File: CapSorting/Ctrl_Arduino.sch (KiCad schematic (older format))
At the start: 18 parts, among them U12 TLP785, U13 TLP785

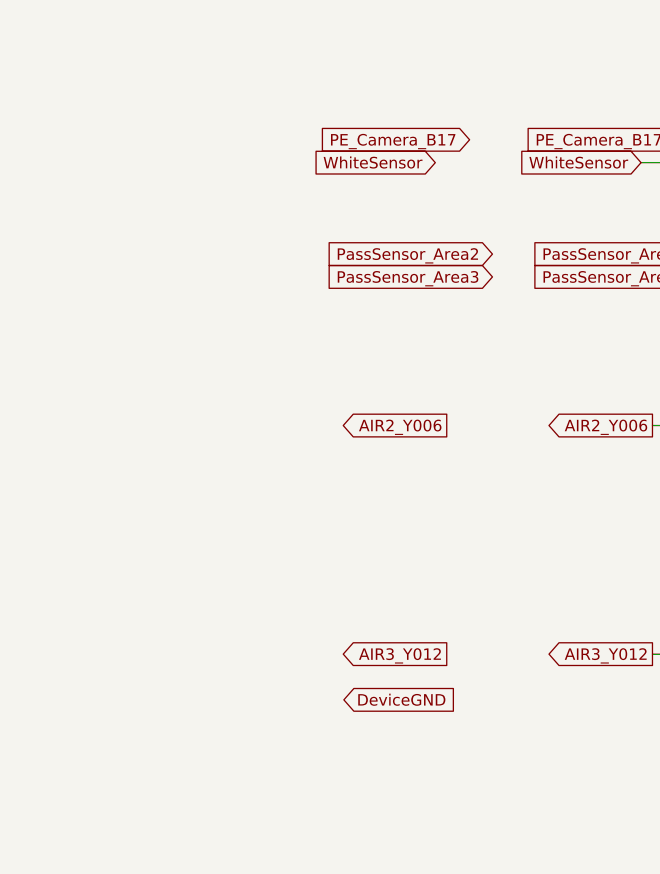
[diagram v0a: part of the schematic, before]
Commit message: Arduino回路図　コネクタ追加
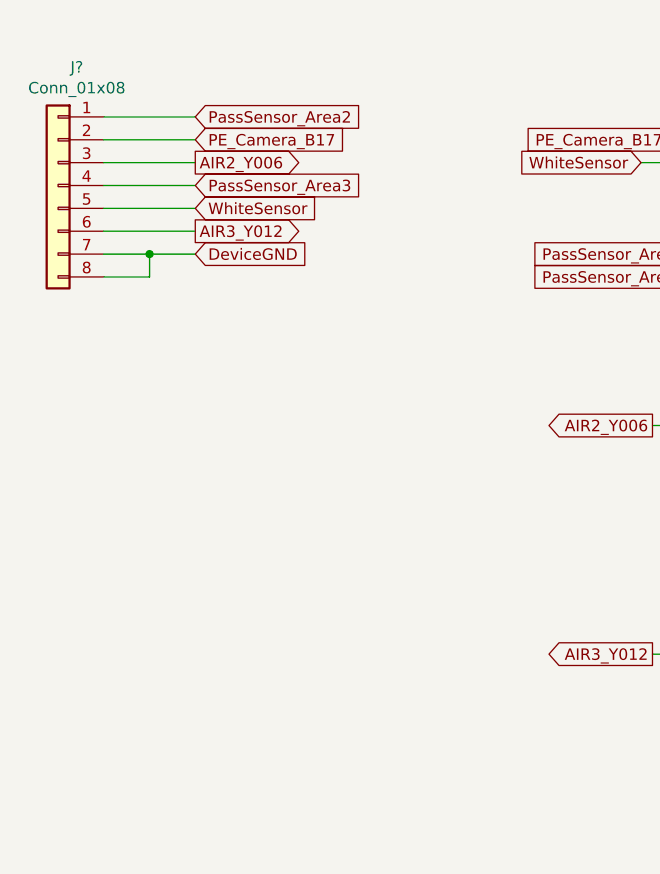
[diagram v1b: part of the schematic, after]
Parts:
- added J?: Conn_01x08, symbol Connector_Generic:Conn_01x08
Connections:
- net AIR2_Y006: now also J?.3 (Pin_3)
- net AIR3_Y012: now also J?.6 (Pin_6)
- net DeviceGND: now also J?.7 (Pin_7), J?.8 (Pin_8)
- net PE_Camera_B17: now also J?.2 (Pin_2)
- net PassSensor_Area2: now also J?.1 (Pin_1)
- net PassSensor_Area3: now also J?.4 (Pin_4)
- net WhiteSensor: now also J?.5 (Pin_5)
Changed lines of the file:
@@
 Text Notes 8350 3000 0    79   ~ 0
 InternalPullUp\nD2-D5\n\n\nInterrupt\nD2-D3
-Text GLabel 2850 3600 0    50   Output ~ 0
+Text GLabel 1750 2450 2    50   Output ~ 0
 AIR2_Y006
-Text GLabel 2800 2450 0    50   Input ~ 0
+Text GLabel 1750 2650 2    50   Input ~ 0
 WhiteSensor
-Text GLabel 2950 2350 0    50   Input ~ 0
+Text GLabel 1750 2350 2    50   Input ~ 0
 PE_Camera_B17
-Text GLabel 3050 2850 0    50   Input ~ 0
+Text GLabel 1750 2250 2    50   Input ~ 0
 PassSensor_Area2
-Text GLabel 3050 2950 0    50   Input ~ 0
+Text GLabel 1750 2550 2    50   Input ~ 0
 PassSensor_Area3
-Text GLabel 2850 4600 0    50   Output ~ 0
+Text GLabel 1750 2750 2    50   Output ~ 0
 AIR3_Y012
-Text GLabel 2400 4800 2    50   Input ~ 0
+Text GLabel 1750 2850 2    50   Input ~ 0
 DeviceGND
+$Comp
+L Connector_Generic:Conn_01x08 J?
+U 1 1 5FE46157
+P 1150 2550
+F 0 "J?" H 1068 3067 50  0000 C CNN
+F 1 "Conn_01x08" H 1068 2976 50  0000 C CNN
+F 2 "" H 1150 2550 50  0001 C CNN
+F 3 "~" H 1150 2550 50  0001 C CNN
+	1    1150 2550
+	-1   0    0    -1
+$EndComp
+Wire Wire Line
+	1350 2850 1550 2850
+Wire Wire Line
+	1550 2850 1550 2950
+Wire Wire Line
+	1350 2950 1550 2950
+Wire Wire Line
+	1750 2850 1550 2850
+Connection ~ 1550 2850
+Wire Wire Line
+	1750 2250 1350 2250
+Wire Wire Line
+	1750 2350 1350 2350
+Wire Wire Line
+	1750 2450 1350 2450
+Wire Wire Line
+	1750 2550 1350 2550
+Wire Wire Line
+	1750 2650 1350 2650
+Wire Wire Line
+	1750 2750 1350 2750
 $EndSCHEMATC

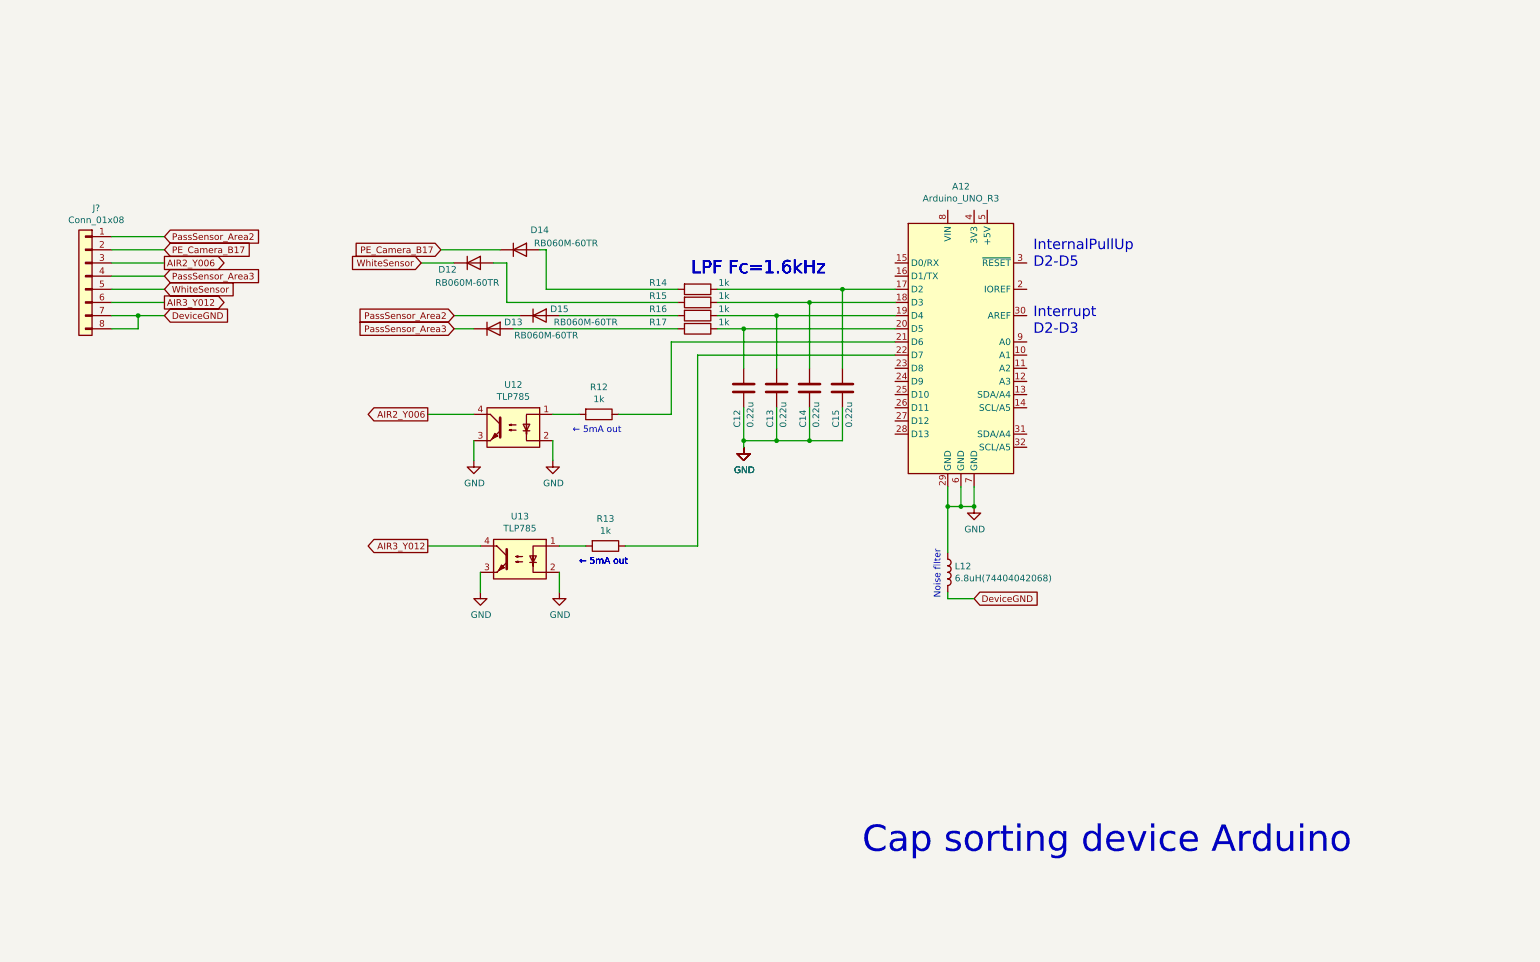
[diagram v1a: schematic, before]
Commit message: Android　シール用追加
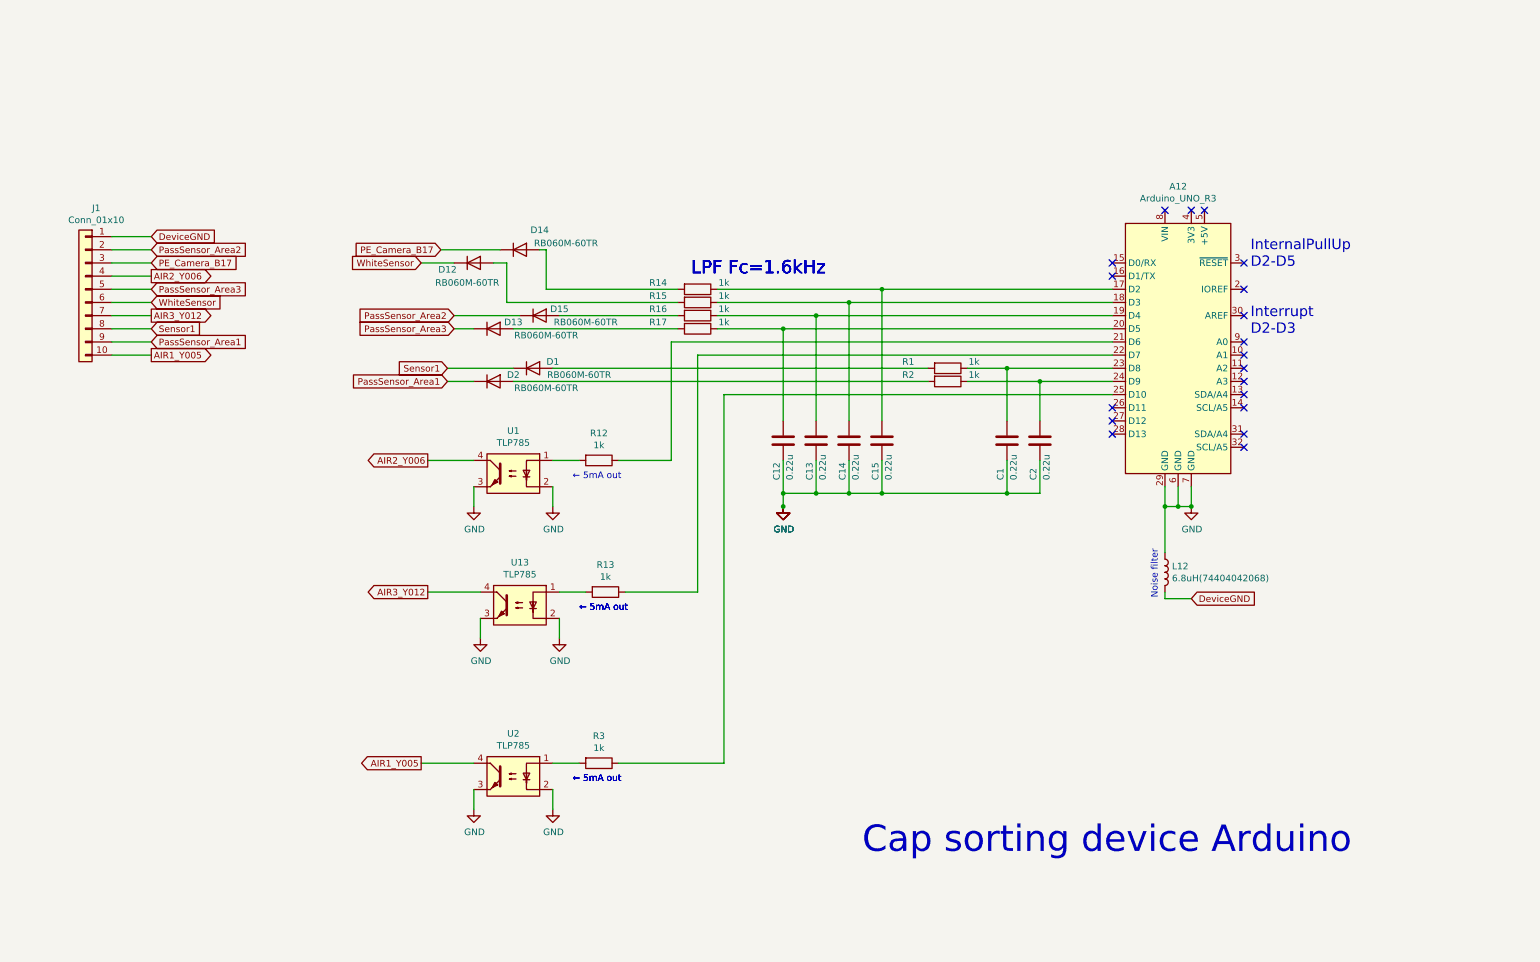
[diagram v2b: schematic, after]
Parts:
- removed J?: Conn_01x08, symbol Connector_Generic:Conn_01x08
- added C1, C2: 0.22u, Resistor_SMD:R_0402_1005Metric, symbol Device:C
- added D1, D2: RB060M-60TR, Diode_SMD:D_1206_3216Metric, symbol Device:D
- added J1: Conn_01x10, JST:S10B-XH-A, symbol Connector_Generic:Conn_01x10
- added R1, R2, R3: 1k, Resistor_SMD:R_0603_1608Metric, symbol Device:R
- added U2: TLP785, Package_DIP:DIP-4_W7.62mm, symbol Isolator:TLP785
- renumbered U12 to U1
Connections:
- net AIR2_Y006: now also J1.4 (Pin_4)
- net AIR3_Y012: now also J1.7 (Pin_7)
- net DeviceGND: now also J1.1 (Pin_1)
- net GND: now also C1.2, C2.2, U2.2, U2.3
- net PE_Camera_B17: now also J1.3 (Pin_3)
- net PassSensor_Area2: now also J1.2 (Pin_2)
- net PassSensor_Area3: now also J1.5 (Pin_5)
- net WhiteSensor: now also J1.6 (Pin_6)
- net at A12.23 (D8): now also C1.1, R1.1
- net at A12.24 (D9): now also C2.1, R2.1
- net at A12.25 (D10): now also R3.1
- new net: R3.2, U2.1
- new net: D1.2 (A), R1.2
- new net: D2.2 (A), R2.2
- new net AIR1_Y005: J1.10 (Pin_10), U2.4
- new net PassSensor_Area1: D2.1 (K), J1.9 (Pin_9)
- new net Sensor1: D1.1 (K), J1.8 (Pin_8)
- no-connect marks 0 -> 19
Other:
- moved on the sheet: A12, C12, C13, C14, C15, L12, R12, R13, U1, U13

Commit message: ガーバデータ追加
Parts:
- added D32, D33, D34: LED, spot:LED1608, symbol Device:LED
- added J33: ZH_B6B-ZR, spot:ZH_B6B-ZR, symbol spot-cache:Connector_Generic_Conn_01x06
- added R39, R40, R41, R42: 100, Resistor_SMD:R_0603_1608Metric, symbol Device:R
- added R43, R44, R47: NC, Resistor_SMD:R_0603_1608Metric, symbol Device:R
- added R45, R46, R48: 2.2k, Resistor_SMD:R_0603_1608Metric, symbol Device:R
- added R49: 0, Resistor_SMD:R_0603_1608Metric, symbol Device:R
- J1: value Conn_01x10 -> S10B-XH-A; footprint JST:S10B-XH-A -> Connector_JST:JST_XH_S10B-XH-A_1x10_P2.50mm_Horizontal
- L12: footprint Ctrl_Arduino:INDPM4040X180N -> CapSorting:INDPM4040X180N
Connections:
- net GND: now also J33.6 (Pin_6)
- net at A12.10 (A1): now also R46.2
- net at A12.11 (A2): now also R39.2, R48.2
- net at A12.12 (A3): now also R40.2
- net at A12.13 (SDA/A4): now also R41.2
- net at A12.14 (SCL/A5): now also R42.2
- net +3V3: now reaches A12.4 (3V3)
- net +3V3: now also D32.2 (A), D33.2 (A), D34.2 (A), R47.2
- net +5V: now reaches A12.5 (+5V)
- net +5V: now also R49.2
- net at A12.9 (A0): now also R45.2
- new net: J33.1 (Pin_1), R43.2, R44.2, R47.1, R49.1
- new net: D32.1 (K), R45.1
- new net: D33.1 (K), R46.1
- new net: D34.1 (K), R48.1
- new net D16_A2: J33.2 (Pin_2), R39.1
- new net D17_A3: J33.3 (Pin_3), R40.1
- new net D18_A4: J33.4 (Pin_4), R41.1, R43.1
- new net D19_A5: J33.5 (Pin_5), R42.1, R44.1
- no-connect marks 19 -> 11
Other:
- note added: "-InternalPullUp\n D2-D5\n-Interrupt\n D2-D3"
- note removed: "InternalPullUp\nD2-D5\n\n\nInterrupt\nD2-D3"
- moved on the sheet: A12, C1, C12, C13, C14, C15, C2, D1, D12, D13, D14, D15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

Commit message: 部品配置図
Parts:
- C1, C2: value 0.22u -> NC
- D1, D2: value RB060M-60TR -> NC
- J33: value ZH_B6B-ZR -> NC(ZH_B6B-ZR)
- R1, R2, R3: value 1k -> NC
- R39, R40, R41, R42: value 100 -> NC
- R49: value 0 -> NC
- U2: value TLP785 -> NC(TLP785)
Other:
- note added: "2020/12/25"
- note added: "Ctrl Arduino"
- note added: "Umeda"
- note removed: "Cap sorting device Arduino"
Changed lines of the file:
@@
 Text Notes 2950 5000 0    50   ~ 0
 ← 5mA out
-Text Notes 7100 6900 0    200  ~ 0
-Cap sorting device Arduino
+Text Notes 8250 6950 0    200  ~ 0
+Ctrl Arduino
 Text GLabel 1800 4850 0    50   Output ~ 0
 AIR3_Y012
@@
 AR Path="/5FEBE07B" Ref="R3"  Part="1"
 F 0 "R3" V 2893 6150 50  0000 C CNN
-F 1 "1k" V 2984 6150 50  0000 C CNN
+F 1 "NC" V 2984 6150 50  0000 C CNN
 F 2 "Resistor_SMD:R_0603_1608Metric" V 3030 6150 50  0001 C CNN
 F 3 "~" H 3100 6150 50  0001 C CNN
@@
 AR Path="/5FEBE087" Ref="U2"  Part="1"
 F 0 "U2" H 2450 6575 50  0000 C CNN
-F 1 "TLP785" H 2450 6484 50  0000 C CNN
+F 1 "NC(TLP785)" H 2450 6484 50  0000 C CNN
 F 2 "Package_DIP:DIP-4_W7.62mm" H 2250 6050 50  0001 L CIN
 F 3 "https://toshiba.semicon-storage.com/info/docget.jsp?did=10569&prodName=TLP785" H 2450 6250 50  0001 L CNN
@@
 AR Path="/5FED1BC7" Ref="C2"  Part="1"
 F 0 "C2" V 5950 3400 50  0000 L CNN
-F 1 "0.22u" V 6050 3400 50  0000 L CNN
+F 1 "NC" V 6050 3400 50  0000 L CNN
 F 2 "Resistor_SMD:R_0402_1005Metric" H 6038 3550 50  0001 C CNN
 F 3 "~" H 6000 3700 50  0001 C CNN
@@
 AR Path="/5FED291B" Ref="C1"  Part="1"
 F 0 "C1" V 5700 3400 50  0000 L CNN
-F 1 "0.22u" V 5800 3400 50  0000 L CNN
+F 1 "NC" V 5800 3400 50  0000 L CNN
 F 2 "Resistor_SMD:R_0402_1005Metric" H 5788 3550 50  0001 C CNN
 F 3 "~" H 5750 3700 50  0001 C CNN
@@
 AR Path="/5FEDD896" Ref="R1"  Part="1"
 F 0 "R1" V 4250 2850 50  0000 C CNN
-F 1 "1k" V 4250 3350 50  0000 C CNN
+F 1 "NC" V 4250 3350 50  0000 C CNN
 F 2 "Resistor_SMD:R_0603_1608Metric" V 4230 3150 50  0001 C CNN
 F 3 "~" H 4300 3150 50  0001 C CNN
@@
 AR Path="/5FEEBF3A" Ref="D1"  Part="1"
 F 0 "D1" H 2750 3200 50  0000 C CNN
-F 1 "RB060M-60TR" H 2950 3100 50  0000 C CNN
+F 1 "NC" H 2750 3100 50  0000 C CNN
 F 2 "Diode_SMD:D_1206_3216Metric" H 2600 3150 50  0001 C CNN
 F 3 "~" H 2600 3150 50  0001 C CNN
@@
 AR Path="/5FEEC2B0" Ref="D2"  Part="1"
 F 0 "D2" H 2450 3300 50  0000 C CNN
-F 1 "RB060M-60TR" H 2700 3200 50  0000 C CNN
+F 1 "NC" H 2450 3200 50  0000 C CNN
 F 2 "Diode_SMD:D_1206_3216Metric" H 2300 3250 50  0001 C CNN
 F 3 "~" H 2300 3250 50  0001 C CNN
@@
 AR Path="/5FEDDF65" Ref="R2"  Part="1"
 F 0 "R2" V 4250 2950 50  0000 C CNN
-F 1 "1k" V 4250 3450 50  0000 C CNN
+F 1 "NC" V 4250 3450 50  0000 C CNN
 F 2 "Resistor_SMD:R_0603_1608Metric" V 4230 3250 50  0001 C CNN
 F 3 "~" H 4300 3250 50  0001 C CNN
@@
 P 10500 5650
 F 0 "J33" H 10580 5642 50  0000 L CNN
-F 1 "ZH_B6B-ZR" H 10580 5551 50  0000 L CNN
+F 1 "NC(ZH_B6B-ZR)" H 10580 5551 50  0000 L CNN
 F 2 "spot:ZH_B6B-ZR" H 10500 5650 50  0001 C CNN
 F 3 "" H 10500 5650 50  0001 C CNN
@@
 AR Path="/5FE7CCFC" Ref="R49"  Part="1"
 F 0 "R49" H 10200 4750 50  0000 C CNN
-F 1 "0" H 10200 4850 50  0000 C CNN
+F 1 "NC" H 10200 4850 50  0000 C CNN
 F 2 "Resistor_SMD:R_0603_1608Metric" V 10280 4750 50  0001 C CNN
 F 3 "~" H 10350 4750 50  0001 C CNN
@@
 AR Path="/5FF9A5F6" Ref="R40"  Part="1"
 F 0 "R40" V 9450 3000 50  0000 C CNN
-F 1 "100" V 9450 3450 50  0000 C CNN
+F 1 "NC" V 9450 3450 50  0000 C CNN
 F 2 "Resistor_SMD:R_0603_1608Metric" V 9430 3250 50  0001 C CNN
 F 3 "~" H 9500 3250 50  0001 C CNN
@@
 AR Path="/5FFA3507" Ref="R41"  Part="1"
 F 0 "R41" V 9450 3100 50  0000 C CNN
-F 1 "100" V 9450 3550 50  0000 C CNN
+F 1 "NC" V 9450 3550 50  0000 C CNN
 F 2 "Resistor_SMD:R_0603_1608Metric" V 9430 3350 50  0001 C CNN
 F 3 "~" H 9500 3350 50  0001 C CNN
@@
 AR Path="/5FFA37B0" Ref="R42"  Part="1"
 F 0 "R42" V 9450 3200 50  0000 C CNN
-F 1 "100" V 9450 3650 50  0000 C CNN
+F 1 "NC" V 9450 3650 50  0000 C CNN
 F 2 "Resistor_SMD:R_0603_1608Metric" V 9430 3450 50  0001 C CNN
 F 3 "~" H 9500 3450 50  0001 C CNN
@@
 AR Path="/5FFB9C55" Ref="R39"  Part="1"
 F 0 "R39" V 9100 2750 50  0000 C CNN
-F 1 "100" V 9200 2800 50  0000 C CNN
+F 1 "NC" V 9200 2800 50  0000 C CNN
 F 2 "Resistor_SMD:R_0603_1608Metric" V 9230 2800 50  0001 C CNN
 F 3 "~" H 9300 2800 50  0001 C CNN
@@
 NoConn ~ 7950 3550
 NoConn ~ 7950 3650
+Text Notes 8350 7650 0    79   ~ 0
+2020/12/25
+Text Notes 10750 7100 0    79   ~ 0
+Umeda
 $EndSCHEMATC
